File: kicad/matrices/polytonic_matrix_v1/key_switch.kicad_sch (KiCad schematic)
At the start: 4 parts, among them SW6 SW_SPST

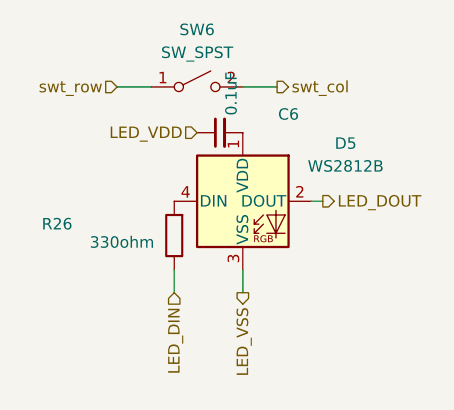
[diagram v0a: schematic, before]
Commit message: [ADD] a barebones structure of the matrix layout for the polytonic characters
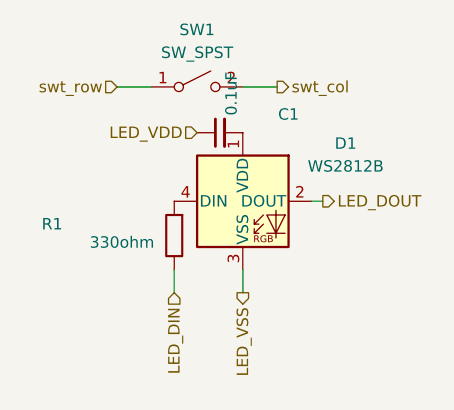
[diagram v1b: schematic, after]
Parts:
- renumbered C6 to C1, D5 to D1, R26 to R1, SW6 to SW1
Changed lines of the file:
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@@
 		(dnp no)
 		(fields_autoplaced yes)
-		(property "Reference" "D5"
+		(property "Reference" "D1"
 			(at 49.53 26.5998 0)
 			(effects
@@
 		)
 		(instances
-			(project "polytonic_greek_keyboard"
-				(path "/cbe25a1b-6c02-43c2-9ff9-ba274c7cf6a2/dc7dc8d0-3fc1-4401-9905-7f0a56042fcf/3567022d-dcc8-4a26-83e7-5efb883a1646/0a734353-c161-4bd5-883e-eaf92a492627"
-					(reference "D5")
-					(unit 1)
-				)
-				(path "/cbe25a1b-6c02-43c2-9ff9-ba274c7cf6a2/dc7dc8d0-3fc1-4401-9905-7f0a56042fcf/3567022d-dcc8-4a26-83e7-5efb883a1646/5f107f1d-b7cf-41cd-afd8-8e41c5a88225"
-					(reference "D6")
-					(unit 1)
-				)
-				(path "/cbe25a1b-6c02-43c2-9ff9-ba274c7cf6a2/dc7dc8d0-3fc1-4401-9905-7f0a56042fcf/3567022d-dcc8-4a26-83e7-5efb883a1646/6fe76989-dc92-4d30-a709-538a22e097b7"
-					(reference "D7")
-					(unit 1)
-				)
-				(path "/cbe25a1b-6c02-43c2-9ff9-ba274c7cf6a2/dc7dc8d0-3fc1-4401-9905-7f0a56042fcf/3567022d-dcc8-4a26-83e7-5efb883a1646/85dfdcb0-9a07-4e64-aafd-2caa92dd5075"
-					(reference "D8")
+			(project "polytonic_matrix_v1"
+				(path "/cbe25a1b-6c02-43c2-9ff9-ba274c7cf6a2/2ba728b0-177f-4c83-8796-28b399b3564a/0a734353-c161-4bd5-883e-eaf92a492627"
+					(reference "D1")
+					(unit 1)
+				)
+				(path "/cbe25a1b-6c02-43c2-9ff9-ba274c7cf6a2/2ba728b0-177f-4c83-8796-28b399b3564a/5f107f1d-b7cf-41cd-afd8-8e41c5a88225"
+					(reference "D2")
+					(unit 1)
+				)
+				(path "/cbe25a1b-6c02-43c2-9ff9-ba274c7cf6a2/2ba728b0-177f-4c83-8796-28b399b3564a/6fe76989-dc92-4d30-a709-538a22e097b7"
+					(reference "D3")
+					(unit 1)
+				)
+				(path "/cbe25a1b-6c02-43c2-9ff9-ba274c7cf6a2/2ba728b0-177f-4c83-8796-28b399b3564a/85dfdcb0-9a07-4e64-aafd-2caa92dd5075"
+					(reference "D4")
 					(unit 1)
 				)
@@
 		(dnp no)
 		(fields_autoplaced yes)
-		(property "Reference" "SW6"
+		(property "Reference" "SW1"
 			(at 33.02 13.97 0)
 			(effects
@@
 		)
 		(instances
-			(project "polytonic_greek_keyboard"
-				(path "/cbe25a1b-6c02-43c2-9ff9-ba274c7cf6a2/dc7dc8d0-3fc1-4401-9905-7f0a56042fcf/3567022d-dcc8-4a26-83e7-5efb883a1646/0a734353-c161-4bd5-883e-eaf92a492627"
-					(reference "SW6")
-					(unit 1)
-				)
-				(path "/cbe25a1b-6c02-43c2-9ff9-ba274c7cf6a2/dc7dc8d0-3fc1-4401-9905-7f0a56042fcf/3567022d-dcc8-4a26-83e7-5efb883a1646/5f107f1d-b7cf-41cd-afd8-8e41c5a88225"
-					(reference "SW7")
-					(unit 1)
-				)
-				(path "/cbe25a1b-6c02-43c2-9ff9-ba274c7cf6a2/dc7dc8d0-3fc1-4401-9905-7f0a56042fcf/3567022d-dcc8-4a26-83e7-5efb883a1646/6fe76989-dc92-4d30-a709-538a22e097b7"
-					(reference "SW8")
-					(unit 1)
-				)
-				(path "/cbe25a1b-6c02-43c2-9ff9-ba274c7cf6a2/dc7dc8d0-3fc1-4401-9905-7f0a56042fcf/3567022d-dcc8-4a26-83e7-5efb883a1646/85dfdcb0-9a07-4e64-aafd-2caa92dd5075"
-					(reference "SW9")
+			(project "polytonic_matrix_v1"
+				(path "/cbe25a1b-6c02-43c2-9ff9-ba274c7cf6a2/2ba728b0-177f-4c83-8796-28b399b3564a/0a734353-c161-4bd5-883e-eaf92a492627"
+					(reference "SW1")
+					(unit 1)
+				)
+				(path "/cbe25a1b-6c02-43c2-9ff9-ba274c7cf6a2/2ba728b0-177f-4c83-8796-28b399b3564a/5f107f1d-b7cf-41cd-afd8-8e41c5a88225"
+					(reference "SW2")
+					(unit 1)
+				)
+				(path "/cbe25a1b-6c02-43c2-9ff9-ba274c7cf6a2/2ba728b0-177f-4c83-8796-28b399b3564a/6fe76989-dc92-4d30-a709-538a22e097b7"
+					(reference "SW3")
+					(unit 1)
+				)
+				(path "/cbe25a1b-6c02-43c2-9ff9-ba274c7cf6a2/2ba728b0-177f-4c83-8796-28b399b3564a/85dfdcb0-9a07-4e64-aafd-2caa92dd5075"
+					(reference "SW4")
 					(unit 1)
 				)
@@
 		(on_board yes)
 		(dnp no)
-		(property "Reference" "C6"
+		(property "Reference" "C1"
 			(at 43.18 23.368 90)
 			(effects
@@
 		)
 		(instances
-			(project "polytonic_greek_keyboard"
-				(path "/cbe25a1b-6c02-43c2-9ff9-ba274c7cf6a2/dc7dc8d0-3fc1-4401-9905-7f0a56042fcf/3567022d-dcc8-4a26-83e7-5efb883a1646/0a734353-c161-4bd5-883e-eaf92a492627"
-					(reference "C6")
-					(unit 1)
-				)
-				(path "/cbe25a1b-6c02-43c2-9ff9-ba274c7cf6a2/dc7dc8d0-3fc1-4401-9905-7f0a56042fcf/3567022d-dcc8-4a26-83e7-5efb883a1646/5f107f1d-b7cf-41cd-afd8-8e41c5a88225"
-					(reference "C7")
-					(unit 1)
-				)
-				(path "/cbe25a1b-6c02-43c2-9ff9-ba274c7cf6a2/dc7dc8d0-3fc1-4401-9905-7f0a56042fcf/3567022d-dcc8-4a26-83e7-5efb883a1646/6fe76989-dc92-4d30-a709-538a22e097b7"
-					(reference "C8")
-					(unit 1)
-				)
-				(path "/cbe25a1b-6c02-43c2-9ff9-ba274c7cf6a2/dc7dc8d0-3fc1-4401-9905-7f0a56042fcf/3567022d-dcc8-4a26-83e7-5efb883a1646/85dfdcb0-9a07-4e64-aafd-2caa92dd5075"
-					(reference "C9")
+			(project "polytonic_matrix_v1"
+				(path "/cbe25a1b-6c02-43c2-9ff9-ba274c7cf6a2/2ba728b0-177f-4c83-8796-28b399b3564a/0a734353-c161-4bd5-883e-eaf92a492627"
+					(reference "C1")
+					(unit 1)
+				)
+				(path "/cbe25a1b-6c02-43c2-9ff9-ba274c7cf6a2/2ba728b0-177f-4c83-8796-28b399b3564a/5f107f1d-b7cf-41cd-afd8-8e41c5a88225"
+					(reference "C2")
+					(unit 1)
+				)
+				(path "/cbe25a1b-6c02-43c2-9ff9-ba274c7cf6a2/2ba728b0-177f-4c83-8796-28b399b3564a/6fe76989-dc92-4d30-a709-538a22e097b7"
+					(reference "C3")
+					(unit 1)
+				)
+				(path "/cbe25a1b-6c02-43c2-9ff9-ba274c7cf6a2/2ba728b0-177f-4c83-8796-28b399b3564a/85dfdcb0-9a07-4e64-aafd-2caa92dd5075"
+					(reference "C4")
 					(unit 1)
 				)
@@
 		(on_board yes)
 		(dnp no)
-		(property "Reference" "R26"
+		(property "Reference" "R1"
 			(at 15.748 35.56 90)
 			(effects
@@
 		)
 		(instances
-			(project "polytonic_greek_keyboard"
-				(path "/cbe25a1b-6c02-43c2-9ff9-ba274c7cf6a2/dc7dc8d0-3fc1-4401-9905-7f0a56042fcf/3567022d-dcc8-4a26-83e7-5efb883a1646/0a734353-c161-4bd5-883e-eaf92a492627"
-					(reference "R26")
-					(unit 1)
-				)
-				(path "/cbe25a1b-6c02-43c2-9ff9-ba274c7cf6a2/dc7dc8d0-3fc1-4401-9905-7f0a56042fcf/3567022d-dcc8-4a26-83e7-5efb883a1646/5f107f1d-b7cf-41cd-afd8-8e41c5a88225"
-					(reference "R27")
-					(unit 1)
-				)
-				(path "/cbe25a1b-6c02-43c2-9ff9-ba274c7cf6a2/dc7dc8d0-3fc1-4401-9905-7f0a56042fcf/3567022d-dcc8-4a26-83e7-5efb883a1646/6fe76989-dc92-4d30-a709-538a22e097b7"
-					(reference "R28")
-					(unit 1)
-				)
-				(path "/cbe25a1b-6c02-43c2-9ff9-ba274c7cf6a2/dc7dc8d0-3fc1-4401-9905-7f0a56042fcf/3567022d-dcc8-4a26-83e7-5efb883a1646/85dfdcb0-9a07-4e64-aafd-2caa92dd5075"
-					(reference "R29")
-					(unit 1)
-				)
+			(project "polytonic_matrix_v1"
+				(path "/cbe25a1b-6c02-43c2-9ff9-ba274c7cf6a2/2ba728b0-177f-4c83-8796-28b399b3564a/0a734353-c161-4bd5-883e-eaf92a492627"
+					(reference "R1")
+					(unit 1)
+				)
+				(path "/cbe25a1b-6c02-43c2-9ff9-ba274c7cf6a2/2ba728b0-177f-4c83-8796-28b399b3564a/5f107f1d-b7cf-41cd-afd8-8e41c5a88225"
+					(reference "R2")
+					(unit 1)
+				)
+				(path "/cbe25a1b-6c02-43c2-9ff9-ba274c7cf6a2/2ba728b0-177f-4c83-8796-28b399b3564a/6fe76989-dc92-4d30-a709-538a22e097b7"
+					(reference "R3")
+					(unit 1)
+				)
+				(path "/cbe25a1b-6c02-43c2-9ff9-ba274c7cf6a2/2ba728b0-177f-4c83-8796-28b399b3564a/85dfdcb0-9a07-4e64-aafd-2caa92dd5075"
+					(reference "R4")
+					(unit 1)
+				)
